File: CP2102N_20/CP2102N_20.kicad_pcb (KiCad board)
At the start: 2 copper layers, 15.2 x 20.3 mm, 20 parts, among them J1 Conn_01x06, P1 USB_C_Plug_USB2.0, U1 CP2102N-A01-GQFN20

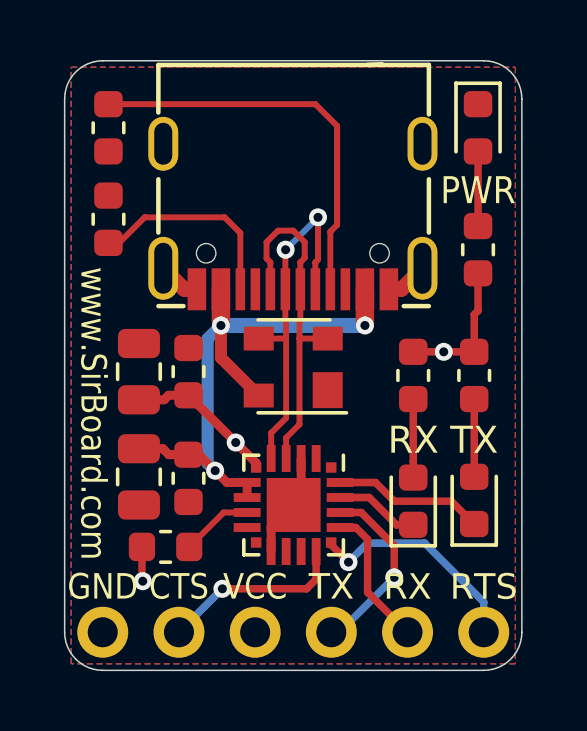
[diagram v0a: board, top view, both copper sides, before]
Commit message: SirUSB Board Revisions
Removed MicroUSB Versions of FT230 and FT231, SolderPaste Layer Adjusted to -0.05mm, Silkscreens optimised, OSHW logo added.
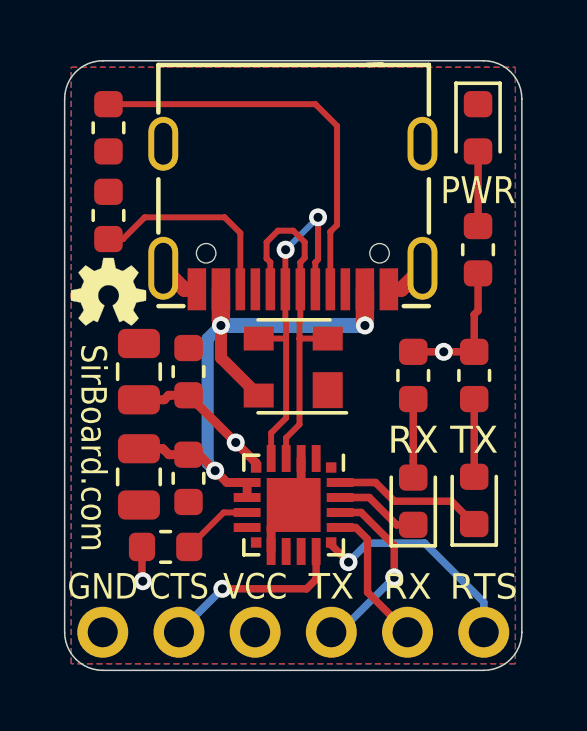
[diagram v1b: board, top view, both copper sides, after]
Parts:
- removed the G*** at (64.6, 43.1)
- added G***: LOGO, logo:OSHW36x26, F.Cu at (58.4, 36.7)
- G***: footprint logo:logo63x89 -> logo:logo76x107
- G***: footprint logo:SirBoard98x31 -> logo:SirBoard127x40
- moved G*** 4.06 mm to (64.6, 42.9)
- moved G*** 2.48 mm to (64.5, 36.3)
- moved R2 0.13 mm to (58.4, 34.2)
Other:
- board text added: "CP2102N USB-UART QFN20"
- board text added: "SirBoard.com"
- board text removed: "CP2102N - QFN20"
- board text removed: "CP2102N USB-UART"
